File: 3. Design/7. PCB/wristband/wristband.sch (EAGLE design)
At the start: 4 parts, among them IC1 MPU-6050, IC2 MAX16150AUT+T, IC4 NRF24L01P-T, IC5 STM32F051K6U6

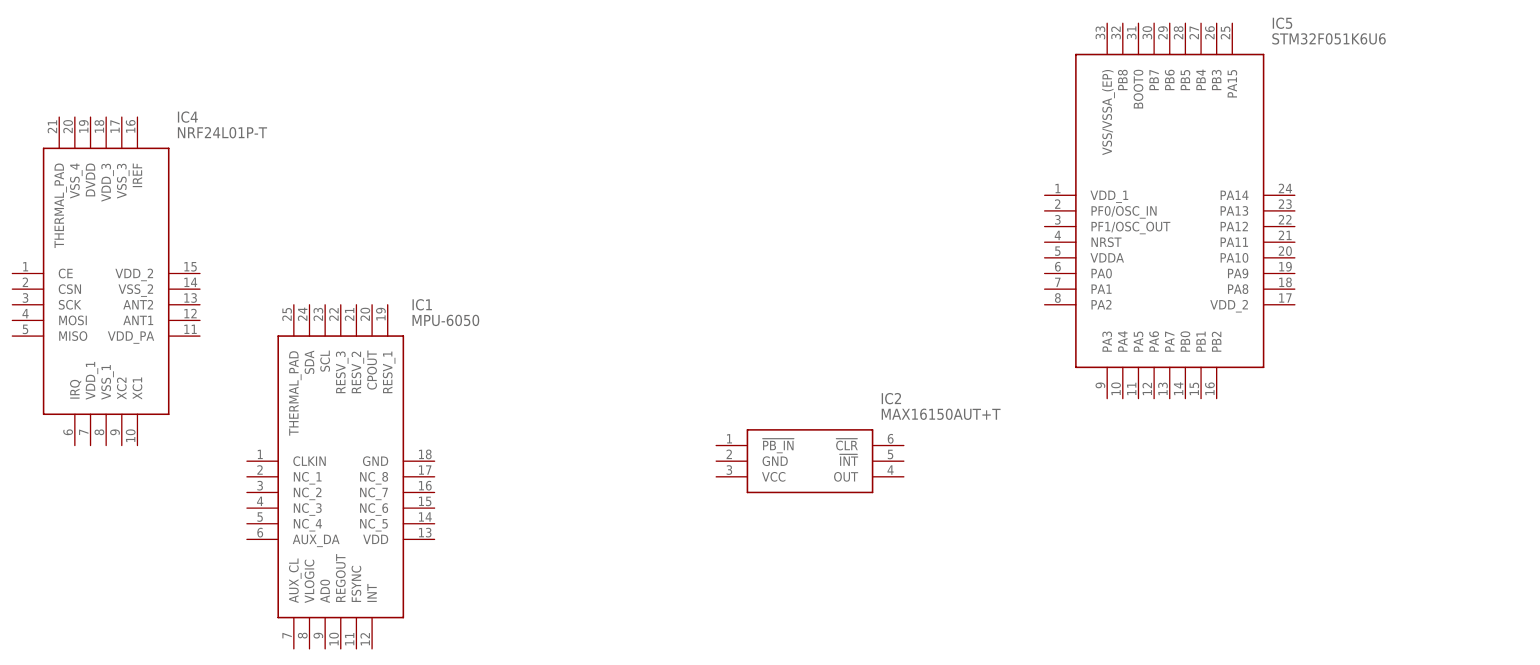
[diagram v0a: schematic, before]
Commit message: ADD|UPDT: Added new antenna library files and initial nRF24L01-balun/filter-antenna interaction sketch
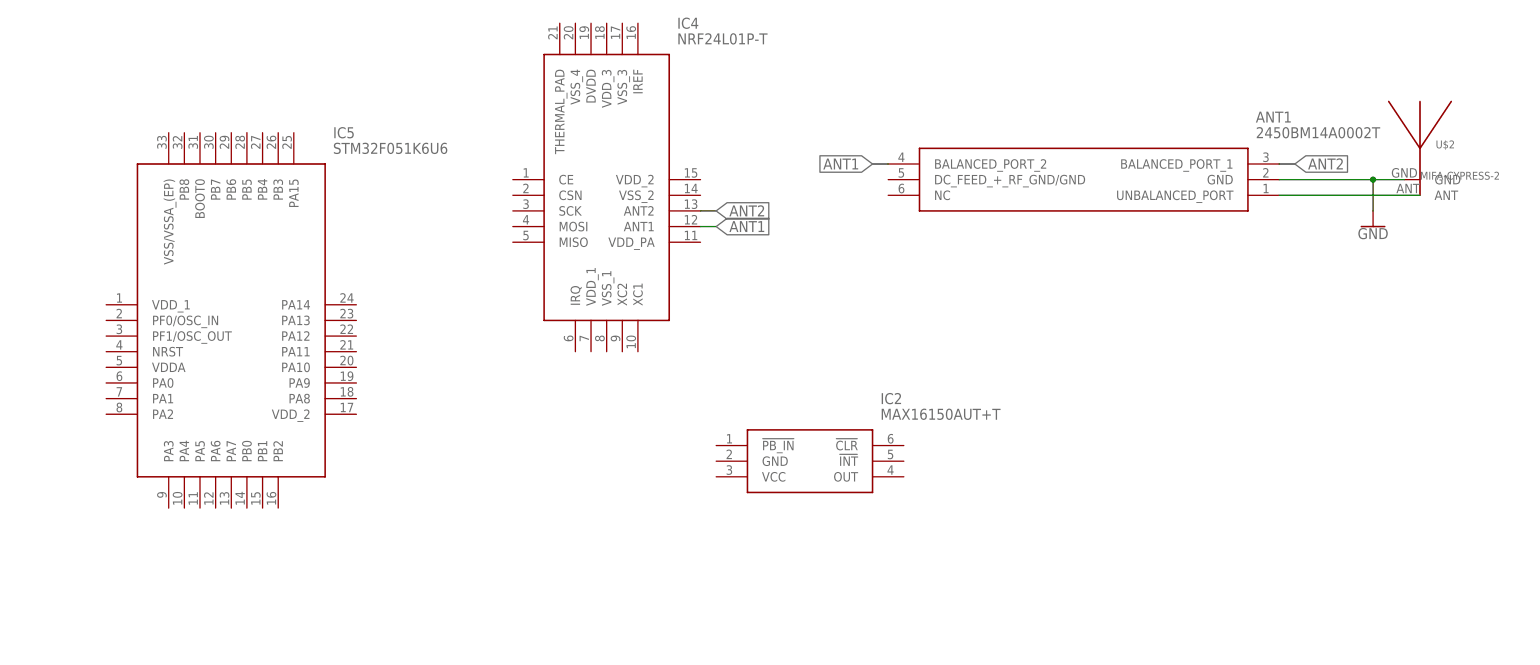
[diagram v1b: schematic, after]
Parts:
- removed IC1: MPU-6050, MPU-6050:MPU-6050
- added ANT1: 2450BM14A0002T, 2450BM14A0002T:2450BM14A0002T
- added U$2: MIFA-CYPRESS-2, MIFA:MIFA-CYPRESS-2
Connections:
- new net ANT1: ANT1.BALANCED_PORT_2, IC4.ANT1
- new net ANT2: ANT1.BALANCED_PORT_1, IC4.ANT2
- new net GND: ANT1.GND, U$2.GND
- new net N$1: ANT1.UNBALANCED_PORT, U$2.ANT
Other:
- moved on the sheet: IC4, IC5
